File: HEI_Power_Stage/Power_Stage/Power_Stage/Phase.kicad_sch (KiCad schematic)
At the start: 36 parts, among them IC1 ACS730KLCTR-65ABT, Q1 EPC2304ENGRT, Q2 EPC2304ENGRT, U2 MP18831-4AGY

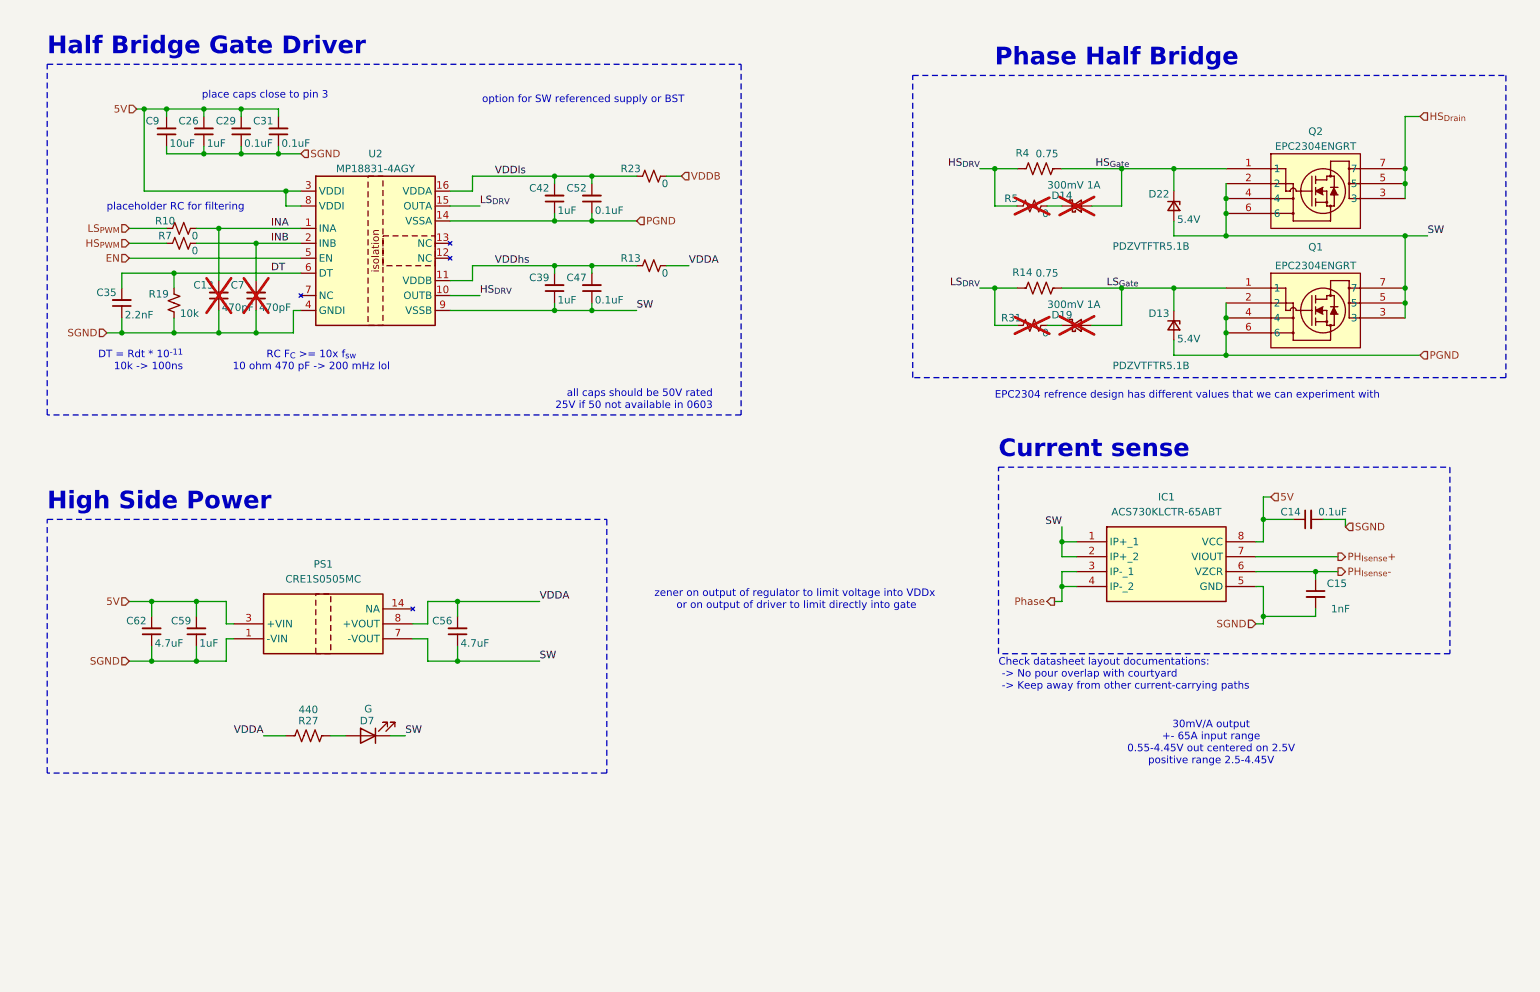
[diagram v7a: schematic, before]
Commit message: allegro gate driver version schematic overhall and layout
layout and routing almost complete for allegro gate drivers
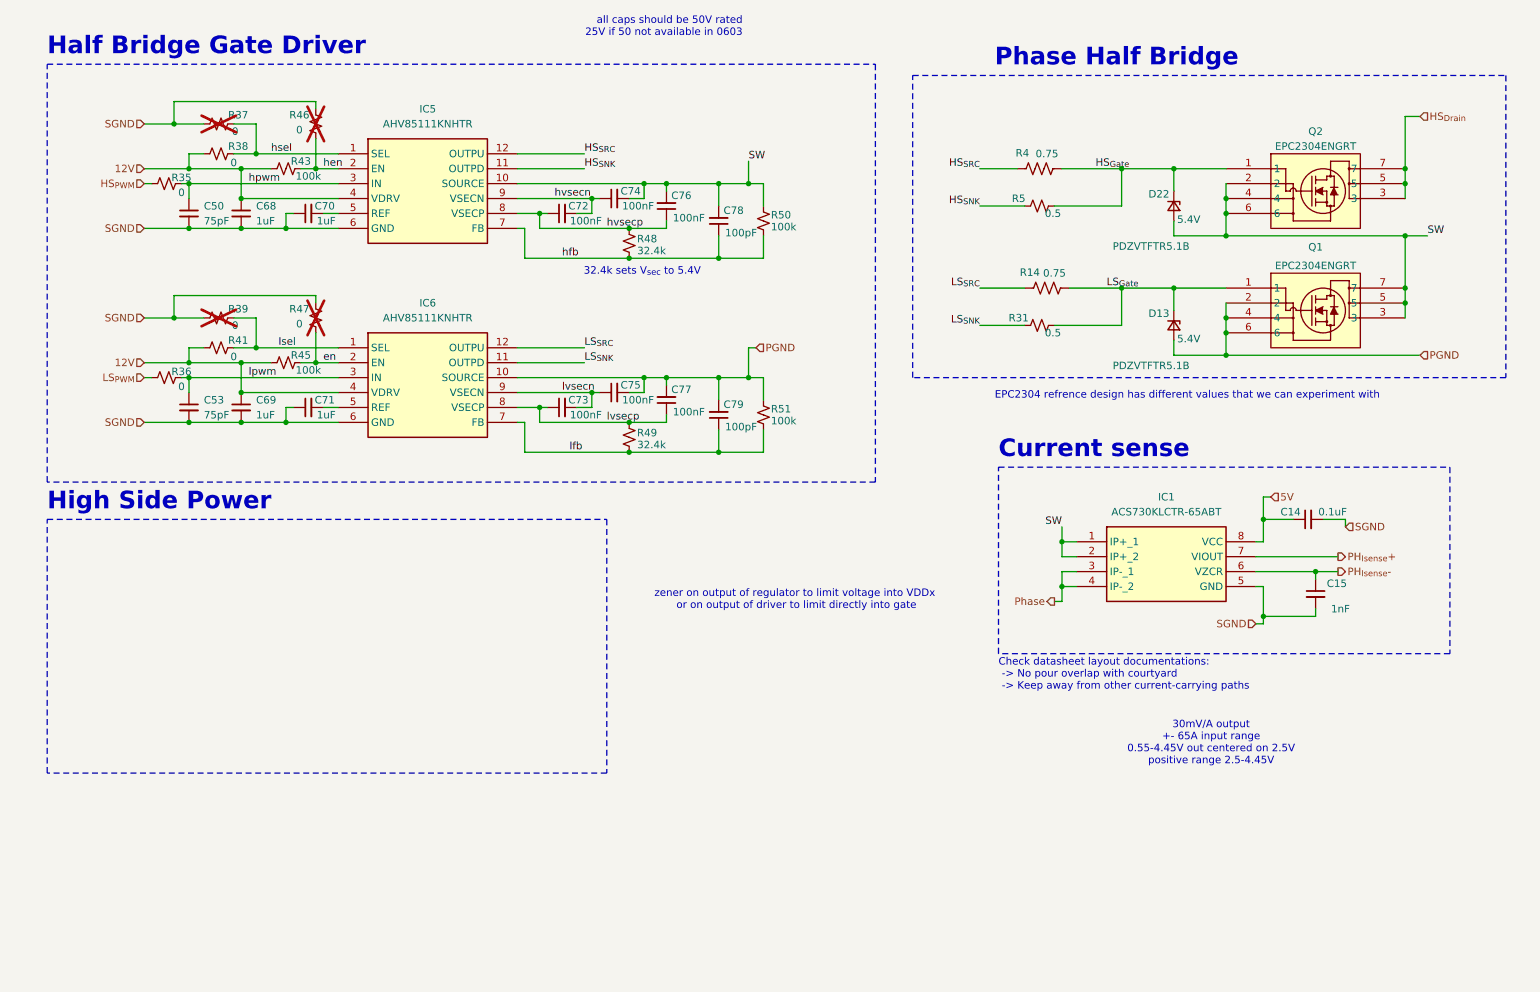
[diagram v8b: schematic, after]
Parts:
- removed C13, C7: 470pF, Capacitor_SMD:C_0603_1608Metric_Pad1.08x0.95mm_HandSolder, symbol Device:C_Small
- removed C26, C39, C42, C59: 1uF, Capacitor_SMD:C_0603_1608Metric_Pad1.08x0.95mm_HandSolder, symbol Device:C_Small
- removed C29, C31, C47, C52: 0.1uF, Capacitor_SMD:C_0603_1608Metric_Pad1.08x0.95mm_HandSolder, symbol Device:C_Small
- removed C35: 2.2nF, Capacitor_SMD:C_0603_1608Metric_Pad1.08x0.95mm_HandSolder, symbol Device:C_Small
- removed C56, C62: 4.7uF, Capacitor_SMD:C_0603_1608Metric_Pad1.08x0.95mm_HandSolder, symbol Device:C_Small
- removed C9: 10uF, Capacitor_SMD:C_0603_1608Metric_Pad1.08x0.95mm_HandSolder, symbol Device:C_Small
- removed D14, D19: 300mV 1A, Diode_SMD:D_SOD-123F, symbol Device:D_Schottky_Small
- removed D7: G, LED_SMD:LED_0603_1608Metric_Pad1.05x0.95mm_HandSolder, symbol Device:LED
- removed PS1: CRE1S0505MC, CRE1S0505MC_KiCad:CRE1S0505MC, symbol CRE1S0505MC:CRE1S0505MC
- removed R10, R13, R23, R7: 0, Resistor_SMD:R_0603_1608Metric_Pad0.98x0.95mm_HandSolder, symbol Device:R_Small_US
- removed R19: 10k, Resistor_SMD:R_0603_1608Metric_Pad0.98x0.95mm_HandSolder, symbol Device:R_Small_US
- removed R27: 440, Resistor_SMD:R_0603_1608Metric_Pad0.98x0.95mm_HandSolder, symbol Device:R_US
- removed U2: MP18831-4AGY, Package_SO:SOIC-16W_7.5x10.3mm_P1.27mm, symbol AHV85111KNHTR:MP18831
- added C50, C53: 75pF, Capacitor_SMD:C_0603_1608Metric_Pad1.08x0.95mm_HandSolder, symbol Device:C_Small
- added C68, C69, C70, C71: 1uF, Capacitor_SMD:C_0603_1608Metric_Pad1.08x0.95mm_HandSolder, symbol Device:C_Small
- added C72, C73, C74, C75, C76, C77: 100nF, Capacitor_SMD:C_0603_1608Metric_Pad1.08x0.95mm_HandSolder, symbol Device:C_Small
- added C78, C79: 100pF, Capacitor_SMD:C_0603_1608Metric_Pad1.08x0.95mm_HandSolder, symbol Device:C_Small
- added IC5, IC6: AHV85111KNHTR, AHV85111_KiCad:AHV85111KNHTR, symbol AHV85111KNHTR:AHV85111KNHTR
- added R35, R36, R37, R38, R39, R41, R46, R47: 0, Resistor_SMD:R_0603_1608Metric_Pad0.98x0.95mm_HandSolder, symbol Device:R_Small_US
- added R43, R45, R50, R51: 100k, Resistor_SMD:R_0603_1608Metric_Pad0.98x0.95mm_HandSolder, symbol Device:R_Small_US
- added R48, R49: 32.4k, Resistor_SMD:R_0603_1608Metric_Pad0.98x0.95mm_HandSolder, symbol Device:R_Small_US
- R14, R4: footprint Resistor_SMD:R_0603_1608Metric_Pad0.98x0.95mm_HandSolder -> Resistor_SMD:R_0805_2012Metric_Pad1.20x1.40mm_HandSolder
- R31, R5: value 0 -> 0.5; footprint Resistor_SMD:R_0603_1608Metric_Pad0.98x0.95mm_HandSolder -> Resistor_SMD:R_0805_2012Metric_Pad1.20x1.40mm_HandSolder; now fitted
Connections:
- net HS_{Gate}: now also R5.2
- net HS_{PWM}: now also R35.1
- net LS_{Gate}: now also R31.2
- net LS_{PWM}: now also R36.1
- net PGND: now also C75.2, C77.2, C79.2, IC6.10 (SOURCE), R51.1
- net SGND: now also C50.2, C53.2, C68.2, C69.2, C70.1, C71.1, IC5.6 (GND), IC6.6 (GND), R37.1, R39.1, R46.2, R47.2
- net SW: now also C74.2, C76.2, C78.2, IC5.10 (SOURCE), R50.1
- net HS_{DRV} renamed HS_{SNK}
- net HS_{SNK}: now also IC5.11 (OUTPD); no longer R4.1
- net LS_{DRV} renamed LS_{SNK}
- net LS_{SNK}: now also IC6.11 (OUTPD); no longer R14.1
- new net: C71.2, IC6.5 (REF)
- new net: C70.2, IC5.5 (REF)
- new net 12V: C68.1, C69.1, IC5.4 (VDRV), IC6.4 (VDRV), R38.1, R41.1, R43.1, R45.1
- new net HS_{SRC}: IC5.12 (OUTPU), R4.1
- new net LS_{SRC}: IC6.12 (OUTPU), R14.1
- new net en: IC6.2 (EN), R45.2, R47.1
- new net hen: IC5.2 (EN), R43.2, R46.1
- new net hfb: C78.1, IC5.7 (FB), R48.1, R50.2
- new net hpwm: C50.1, IC5.3 (IN), R35.2
- new net hsel: IC5.1 (SEL), R37.2, R38.2
- new net hvsecn: C72.2, C74.1, IC5.9 (VSECN)
- new net hvsecp: C72.1, C76.1, IC5.8 (VSECP), R48.2
- new net lfb: C79.1, IC6.7 (FB), R49.1, R51.2
- new net lpwm: C53.1, IC6.3 (IN), R36.2
- new net lsel: IC6.1 (SEL), R39.2, R41.2
- new net lvsecn: C73.2, C75.1, IC6.9 (VSECN)
- new net lvsecp: C73.1, C77.1, IC6.8 (VSECP), R49.2
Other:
- note added: "32.4k sets V_{sec} to 5.4V"
- note removed: "DT = Rdt * 10^{-11} 10k -> 100ns"
- note removed: "RC F_{C} >= 10x f_{sw} 10 ohm 470 pF -> 200 mHz lol"
- note removed: "option for SW referenced supply or BST"
- note removed: "place caps close to pin 3"
- note removed: "placeholder RC for filtering"
- moved on the sheet: R14
